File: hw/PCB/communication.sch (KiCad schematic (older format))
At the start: 4 parts, among them J6 U.FL, U3 RFM69HCW

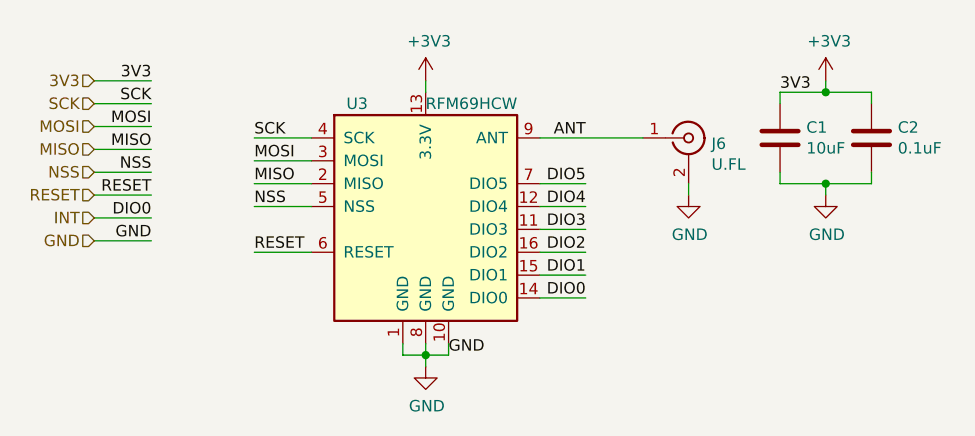
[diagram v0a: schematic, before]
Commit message: FOD's new PCB version.
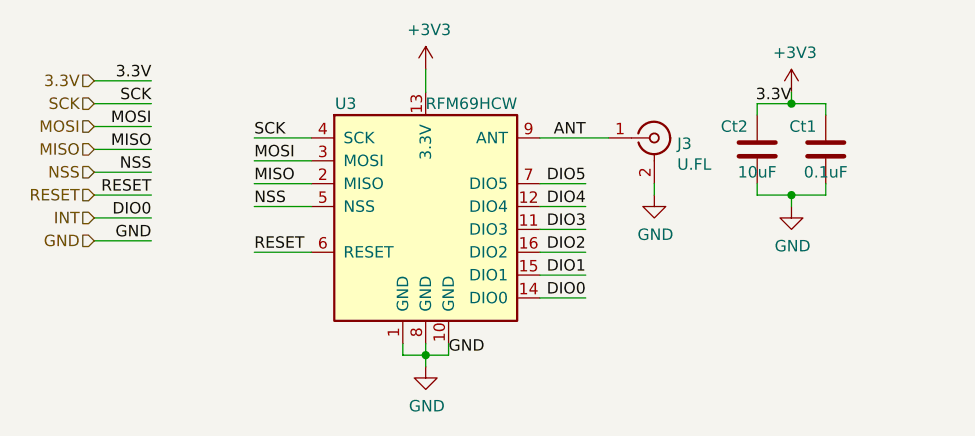
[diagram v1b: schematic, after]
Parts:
- removed C1: 10uF, Capacitor_SMD:C_0603_1608Metric_Pad1.05x0.95mm_HandSolder, symbol Device:C
- removed C2: 0.1uF, Capacitor_SMD:C_0603_1608Metric_Pad1.05x0.95mm_HandSolder, symbol Device:C
- removed J6: U.FL, Connector_Coaxial:U.FL_Hirose_U.FL-R-SMT-1_Vertical, symbol Connector:Conn_Coaxial
- removed U3: RFM69HCW, Transceptor:RFM69HCW, symbol RF_Module:RFM69HCW
- added Ct1: 0.1uF, Capacitor_SMD:C_0603_1608Metric_Pad1.05x0.95mm_HandSolder, symbol Device:C
- added Ct2: 10uF, Capacitor_SMD:C_0603_1608Metric_Pad1.05x0.95mm_HandSolder, symbol Device:C
- added J3: U.FL, Connector_Coaxial:U.FL_Hirose_U.FL-R-SMT-1_Vertical, symbol Connector:Conn_Coaxial
- added U4: RFM69HCW, Transceptor:RFM69HCW, symbol RF_Module:RFM69HCW
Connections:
- net +3V3: now also Ct1.2, Ct2.2, U4.13 (3.3V)
- net ANT: now also J3.1 (In), U4.9 (ANT)
- net DIO1: now also U4.15 (DIO1)
- net DIO2: now also U4.16 (DIO2)
- net DIO3: now also U4.11 (DIO3)
- net DIO4: now also U4.12 (DIO4)
- net DIO5: now also U4.7 (DIO5)
- net GND: now also Ct1.1, Ct2.1, J3.2 (Ext), U4.1 (GND), U4.10 (GND), U4.8 (GND)
- net INT: now also U4.14 (DIO0)
- net MISO: now also U4.2 (MISO)
- net MOSI: now also U4.3 (MOSI)
- net NSS: now also U4.5 (NSS)
- net RESET: now also U4.6 (RESET)
- net SCK: now also U4.4 (SCK)
